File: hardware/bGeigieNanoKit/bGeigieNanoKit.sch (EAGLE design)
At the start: 36 parts, among them T1 2SC1815

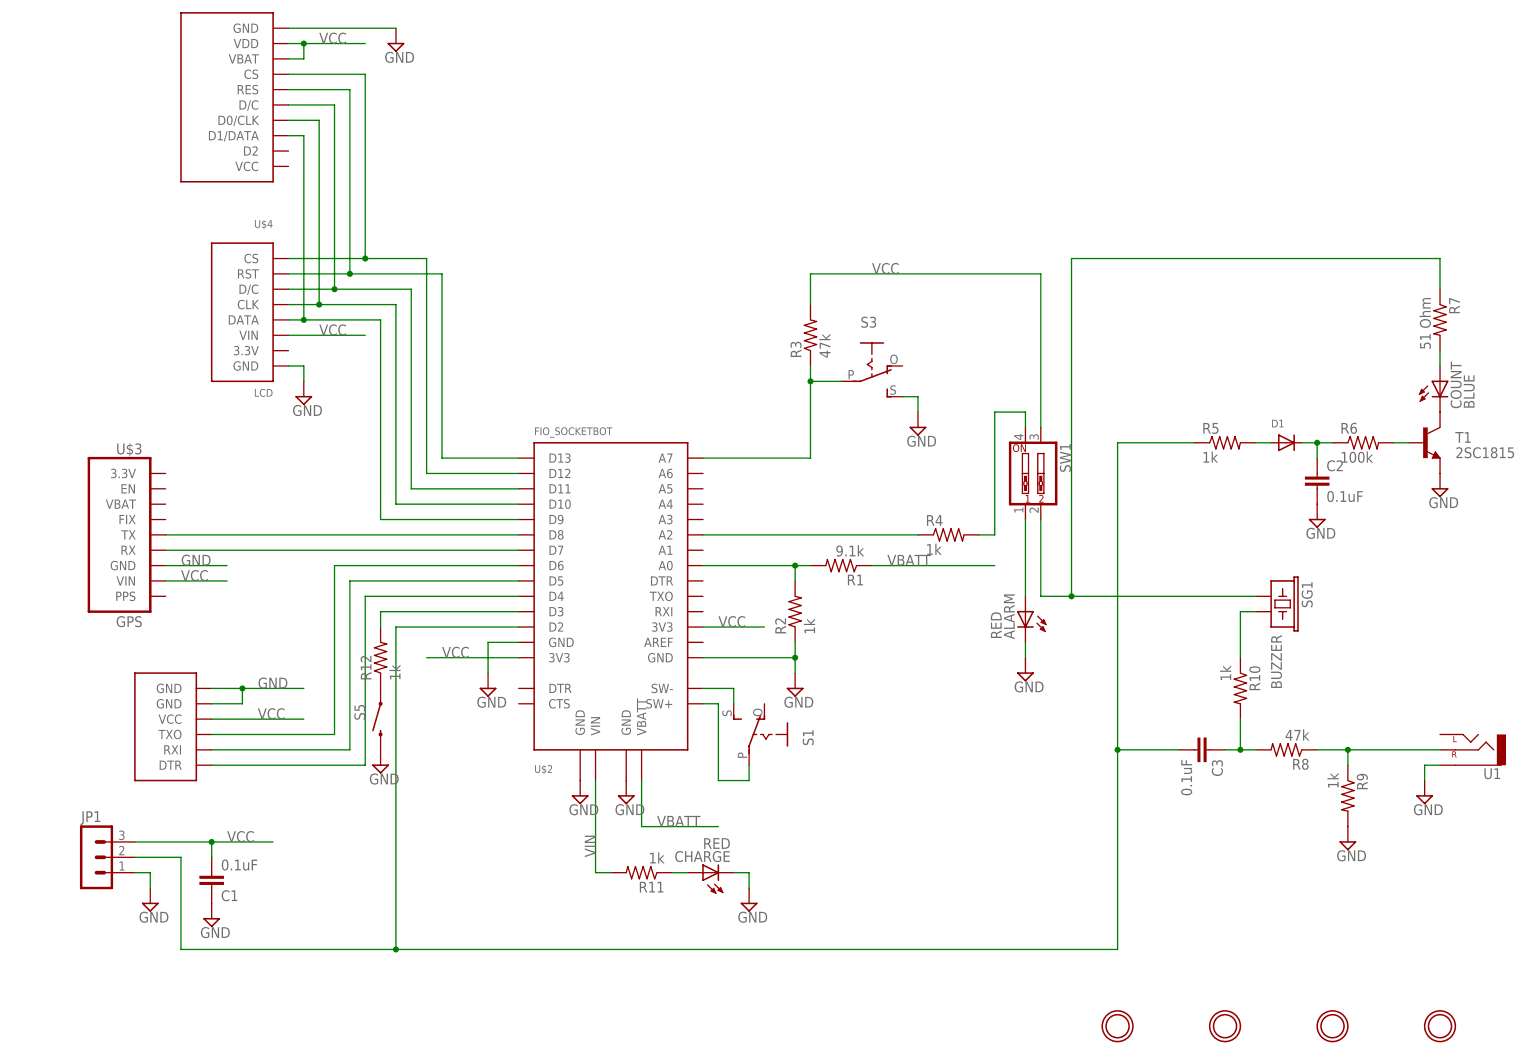
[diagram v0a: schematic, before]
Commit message: gererating outputs for single OLED layout. changigng to toggle switch
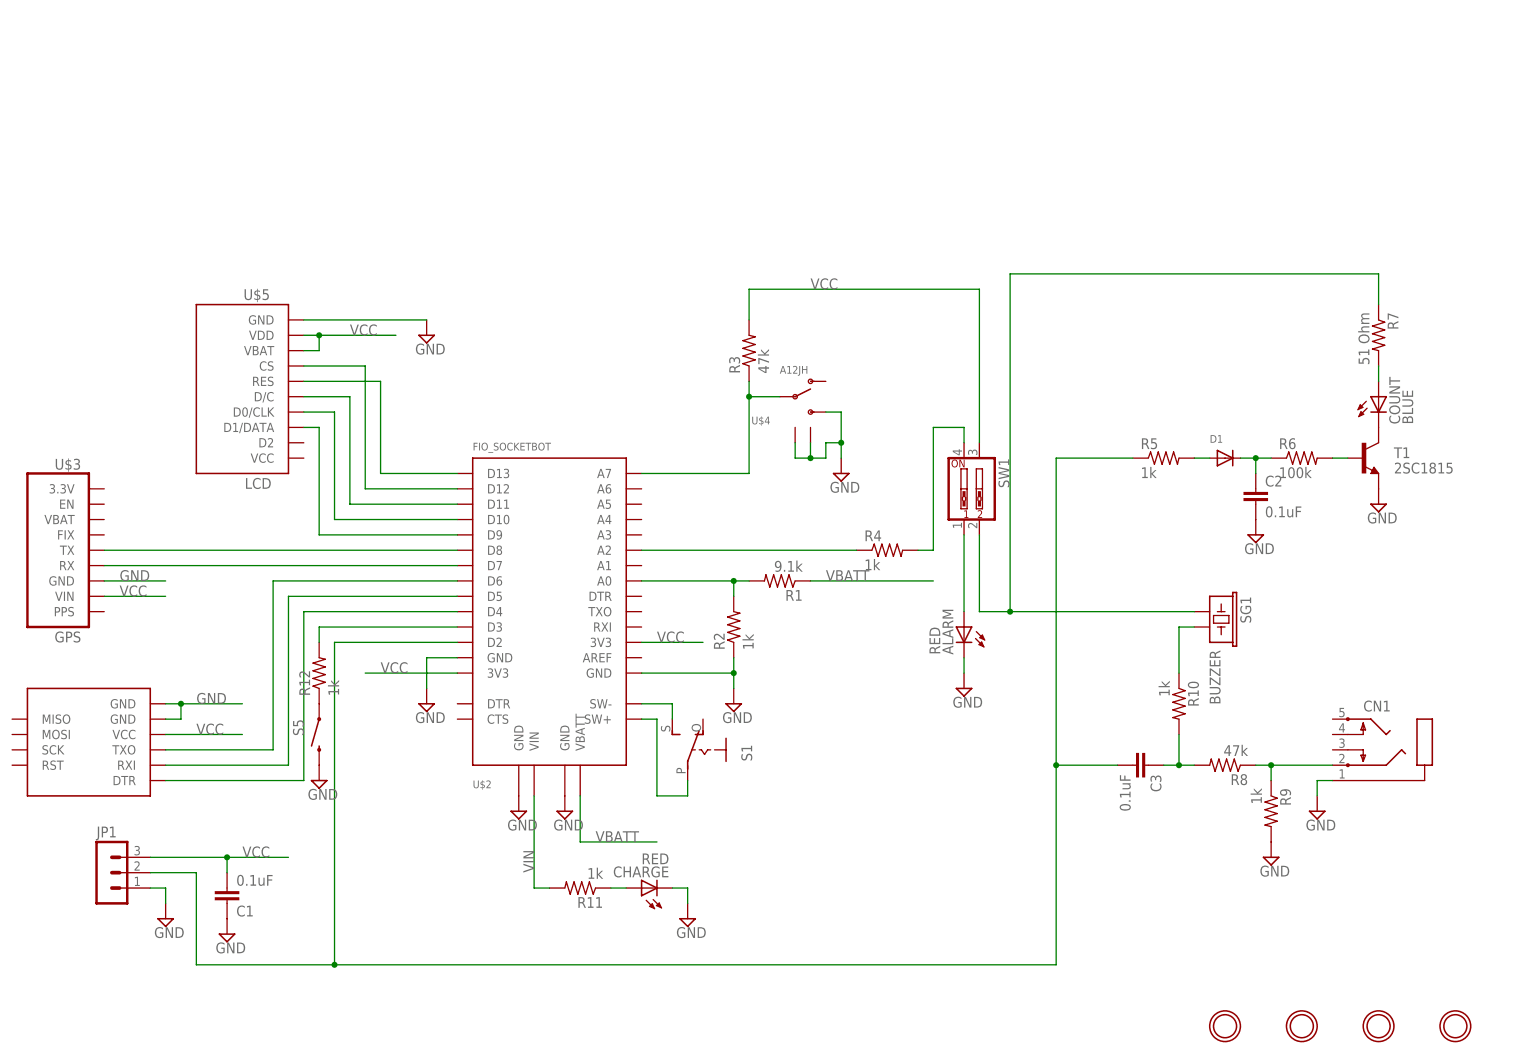
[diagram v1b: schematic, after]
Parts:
- removed S3: (no value), adafruit:EG1218S
- removed U1: (no value), SparkFun:AUDIO-JACK2.5MM
- added CN1: (no value), microbuilder:AUDIO_STEREOJACK
- U$1: value OPENLOG_MINITOP -> OPENLOG; device open_hw_sockets:OPENLOG_MINITOP -> open_hw_sockets:OPENLOG
- U$4: value LCD -> A12JH; device open_hw_sockets:SSD1306_128X32_SPI_LCDTOP -> open_hw_sockets:A12JH
- U$5: value SSD1306_128X64_LCD_MIN -> LCD
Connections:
- net GND: now also CN1.1, U$4.GND@2, U$4.P$3; no longer S3.S, U1.SLEEVE
- net N$1: no longer U$4.DATA
- net N$14: now also U$4.P$2; no longer S3.P
- net N$2: no longer U$4.CLK
- net N$25: now also CN1.2; no longer U1.RIGHT
- net N$3: no longer U$4.D/C
- net N$4: no longer U$4.CS
- net N$5: no longer U$4.RST
- net VCC: no longer U$4.VIN
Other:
- moved on the sheet: ALARM, C1, C2, C3, CHARGE, COUNT, D1, JP1, R1, R10, R11, R12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

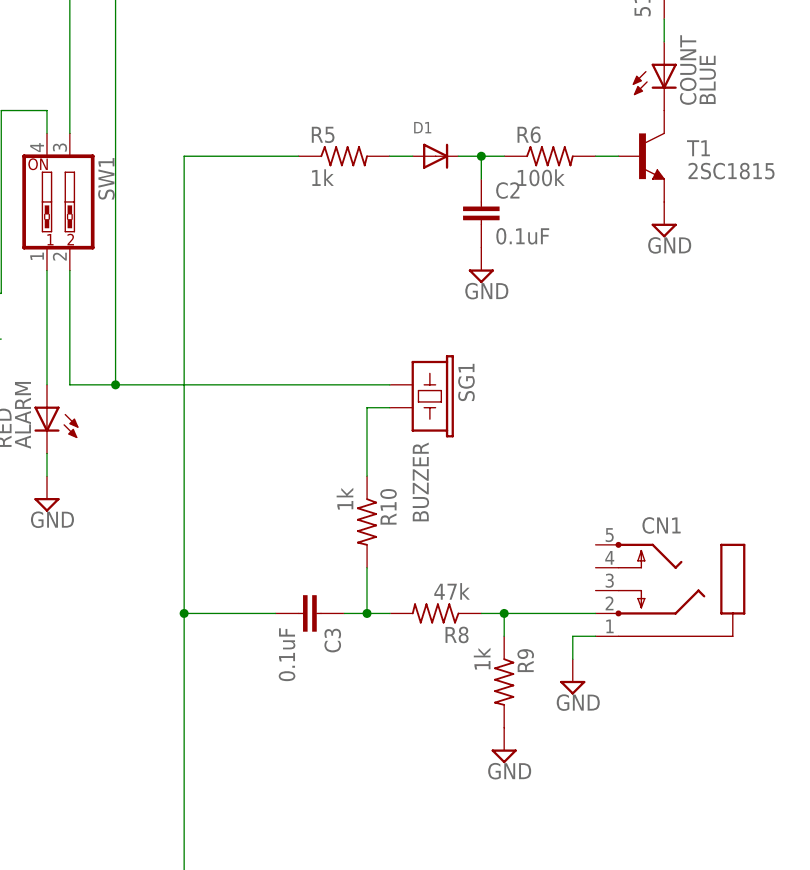
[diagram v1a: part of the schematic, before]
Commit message: Changed R5 and R9 to 4.7 k
For decreasing the load on the IRover output to prevent lower CPM count.
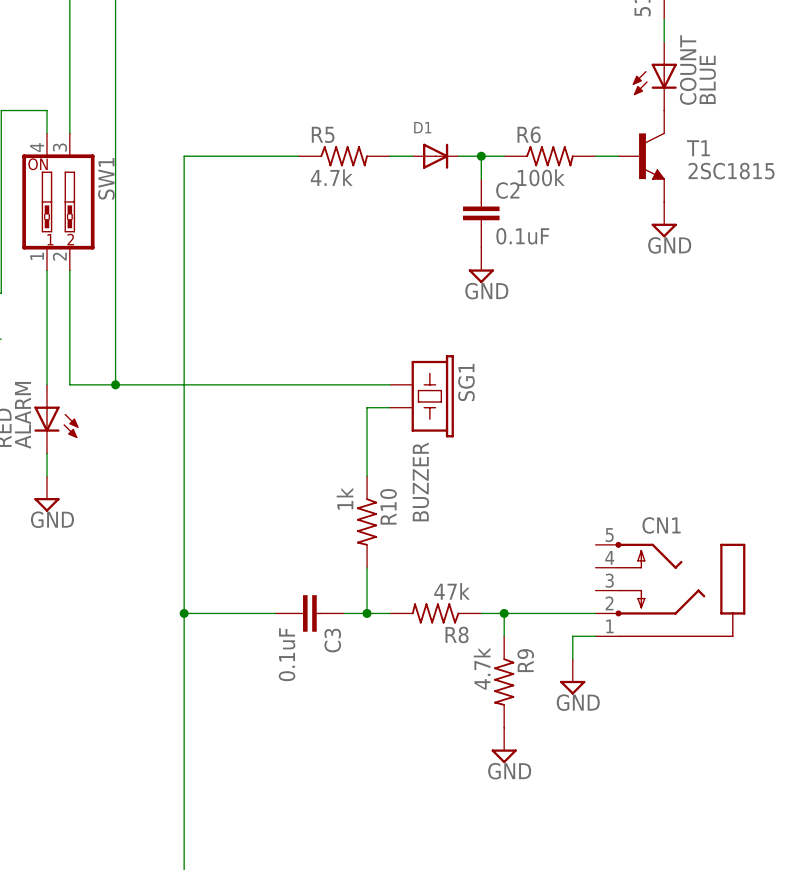
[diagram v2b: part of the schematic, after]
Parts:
- R5, R9: value 1k -> 4.7k
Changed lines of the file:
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@@
 <?xml version="1.0" encoding="utf-8"?>
 <!DOCTYPE eagle SYSTEM "eagle.dtd">
-<eagle version="6.3">
+<eagle version="6.4">
 <drawing>
 <settings>
@@
 <setting verticaltext="up"/>
 </settings>
-<grid distance="0.1" unitdist="inch" unit="inch" style="dots" multiple="1" display="yes" altdistance="0.01" altunitdist="inch" altunit="inch"/>
+<grid distance="0.1" unitdist="inch" unit="inch" style="lines" multiple="1" display="no" altdistance="0.01" altunitdist="inch" altunit="inch"/>
 <layers>
 <layer number="1" name="Top" color="4" fill="1" visible="no" active="no"/>
@@
 <part name="R3" library="rcl" deviceset="R-US_" device="0207/10" value="47k"/>
 <part name="R4" library="rcl" deviceset="R-US_" device="0207/10" value="1k"/>
-<part name="R5" library="rcl" deviceset="R-US_" device="0207/10" value="1k"/>
+<part name="R5" library="rcl" deviceset="R-US_" device="0207/10" value="4.7k"/>
 <part name="R6" library="rcl" deviceset="R-US_" device="0207/10" value="100k"/>
 <part name="R7" library="rcl" deviceset="R-US_" device="0207/10" value="51 Ohm"/>
 <part name="R8" library="rcl" deviceset="R-US_" device="0207/10" value="47k"/>
-<part name="R9" library="rcl" deviceset="R-US_" device="0207/10" value="1k"/>
+<part name="R9" library="rcl" deviceset="R-US_" device="0207/10" value="4.7k"/>
 <part name="R10" library="rcl" deviceset="R-US_" device="0207/10" value="1k"/>
 <part name="SUPPLY1" library="supply2" deviceset="GND" device=""/>
